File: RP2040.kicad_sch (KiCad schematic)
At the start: 19 parts, among them U1 RP2040, Y1 12MHz

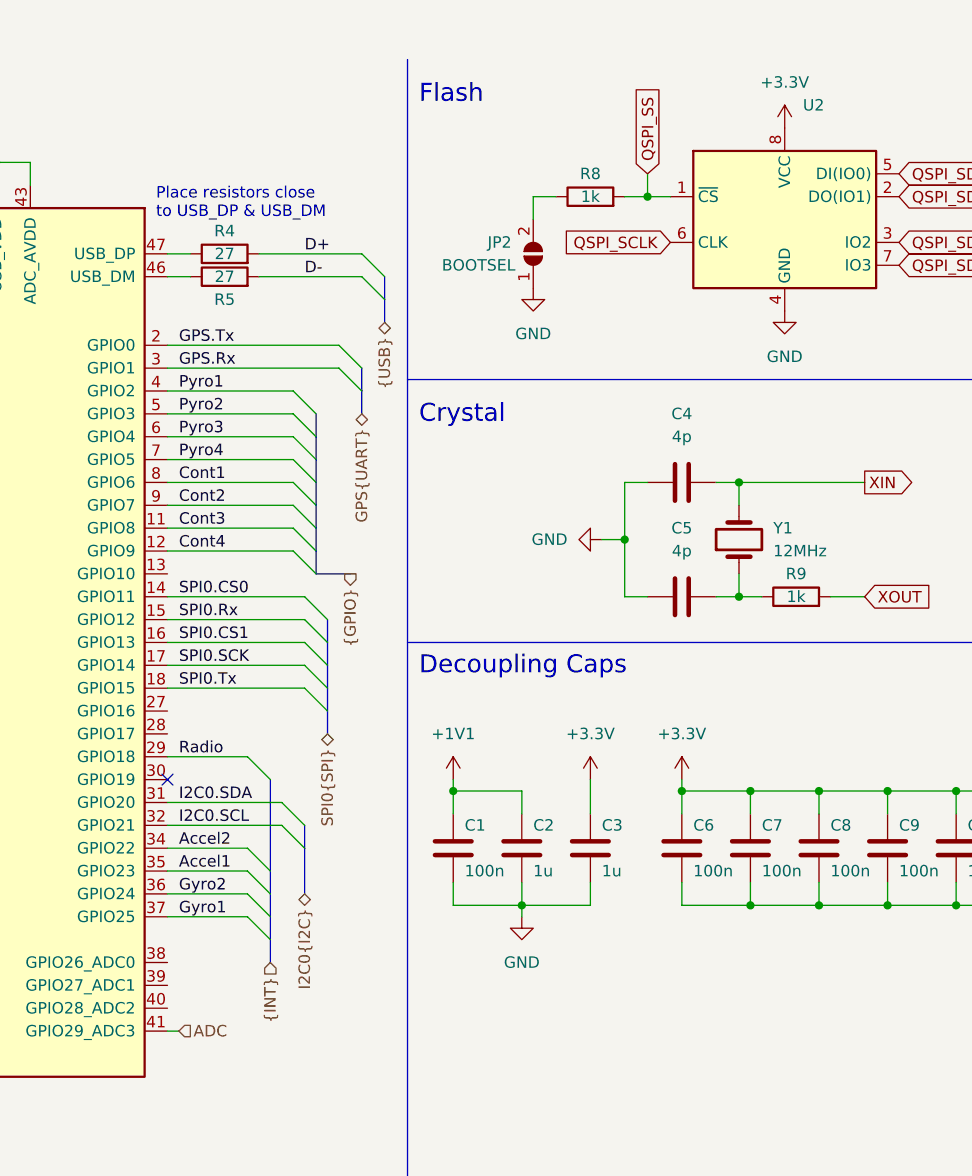
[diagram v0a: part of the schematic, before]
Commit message: Added polyfuse
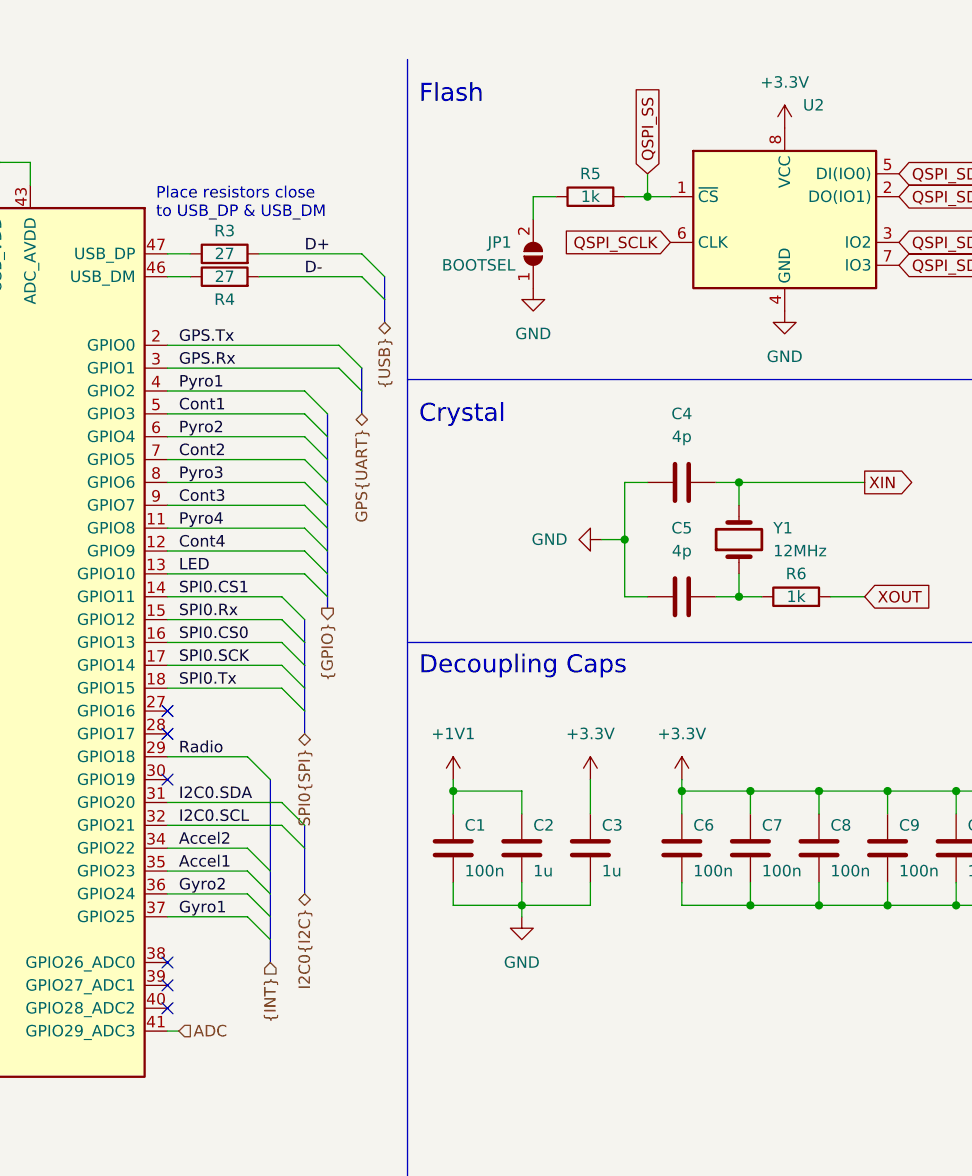
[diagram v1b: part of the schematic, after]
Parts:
- renumbered JP2 to JP1, R4 to R3, R5 to R4, R8 to R5, R9 to R6
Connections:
- net Cont1: now also U1.5 (GPIO3); no longer U1.8 (GPIO6)
- net Cont2: now also U1.7 (GPIO5); no longer U1.9 (GPIO7)
- net Cont3: now also U1.9 (GPIO7); no longer U1.11 (GPIO8)
- net Pyro2: now also U1.6 (GPIO4); no longer U1.5 (GPIO3)
- net Pyro3: now also U1.8 (GPIO6); no longer U1.6 (GPIO4)
- net Pyro4: now also U1.11 (GPIO8); no longer U1.7 (GPIO5)
- net SPI0.CS0: now also U1.16 (GPIO13); no longer U1.14 (GPIO11)
- net SPI0.CS1: now also U1.14 (GPIO11); no longer U1.16 (GPIO13)
- net LED: now reaches U1.13 (GPIO10)
- no-connect marks 5 -> 10

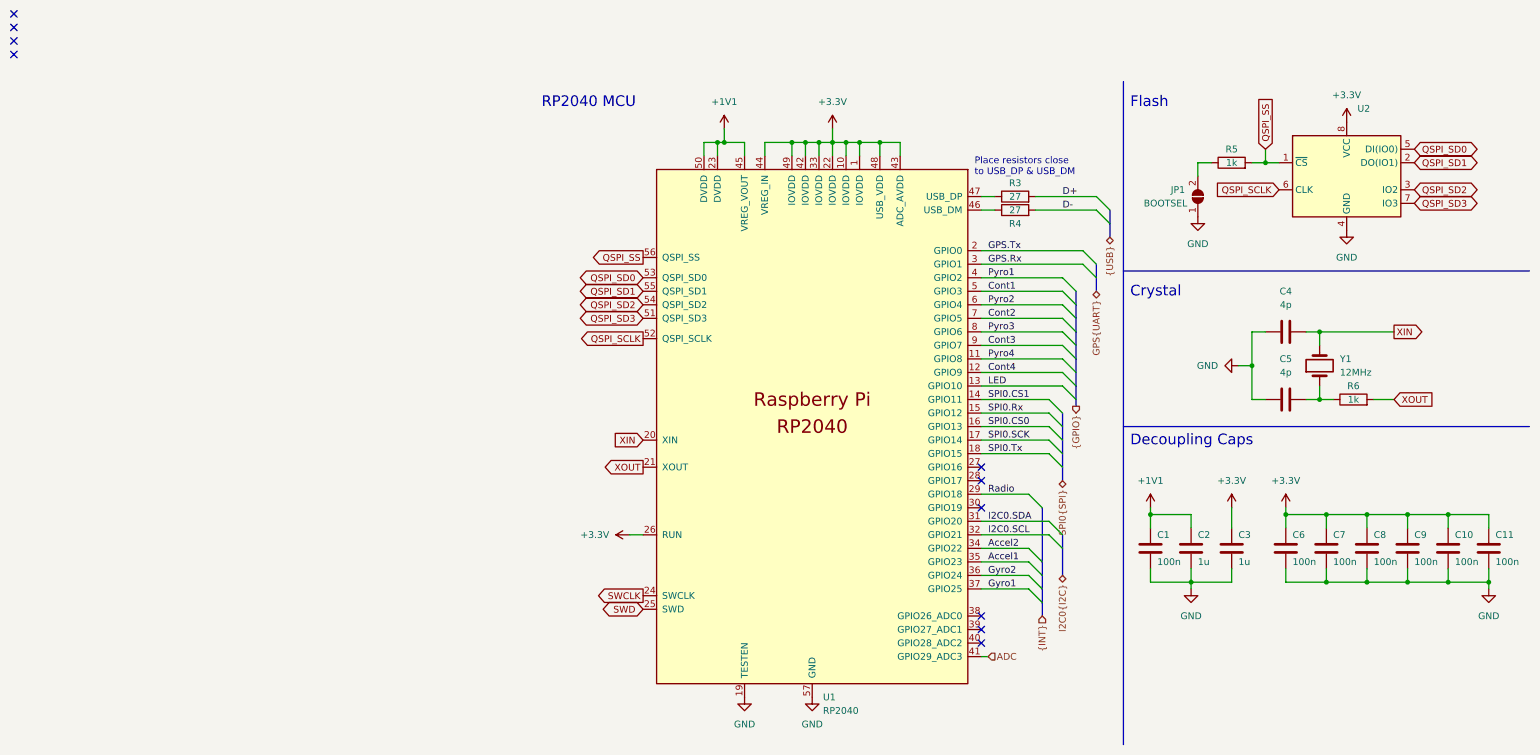
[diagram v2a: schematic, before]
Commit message: Centered RP2040, added mounting hardware, Rearranged radio
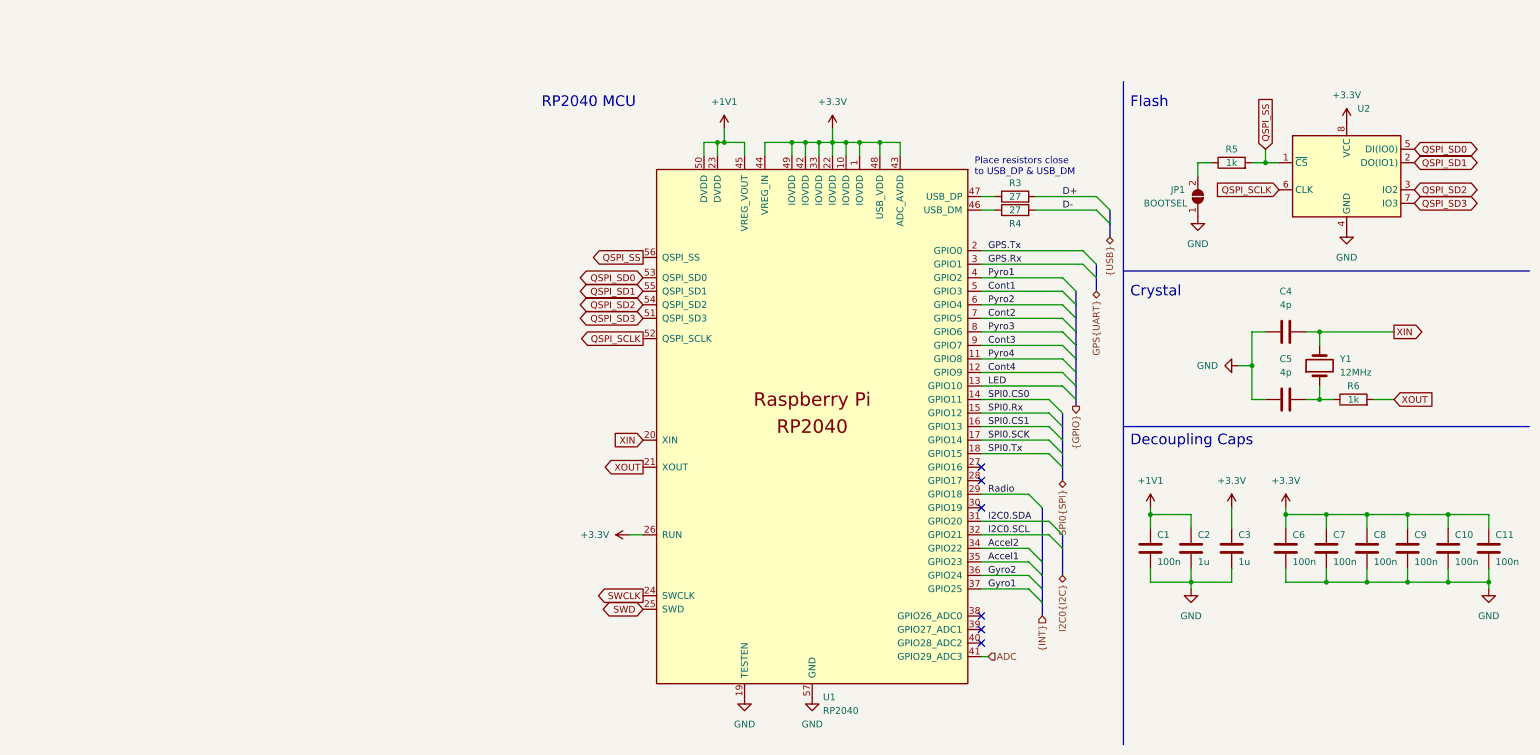
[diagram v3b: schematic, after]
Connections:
- net SPI0.CS0: now also U1.14 (GPIO11); no longer U1.16 (GPIO13)
- net SPI0.CS1: now also U1.16 (GPIO13); no longer U1.14 (GPIO11)
- no-connect marks 10 -> 6
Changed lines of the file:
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@@
   (junction (at 46.99 22.86) (diameter 0) (color 0 0 0 0)
   )
-  (no_connect (at -86.36 1.27))
   (no_connect (at 95.25 91.44))
-  (no_connect (at -86.36 -1.27))
-  (no_connect (at -86.36 3.81))
-  (no_connect (at -86.36 6.35))
   (no_connect (at 95.25 111.76))
   (no_connect (at 95.25 114.3))
@@
     (effects (font (size 1.27 1.27)) (justify left bottom))
   )
-  (label "SPI0.CS1" (at 96.52 71.12 0)
+  (label "SPI0.CS0" (at 96.52 71.12 0)
     (effects (font (size 1.27 1.27)) (justify left bottom))
   )
@@
     (effects (font (size 1.27 1.27)) (justify left bottom))
   )
-  (label "SPI0.CS0" (at 96.52 76.2 0)
+  (label "SPI0.CS1" (at 96.52 76.2 0)
     (effects (font (size 1.27 1.27)) (justify left bottom))
   )
@@
   (symbol (lib_id "power:GND") (at 190.5 106.68 0) (unit 1)
     (in_bom yes) (on_board yes) (fields_autoplaced)
-    (property "Reference" "#PWR015" (id 0) (at 190.5 113.03 0)
+    (property "Reference" "#PWR019" (id 0) (at 190.5 113.03 0)
       (effects (font (size 1.27 1.27)) hide)
     )
@@
   (symbol (lib_id "power:+3.3V") (at 152.4 91.44 0) (unit 1)
     (in_bom yes) (on_board yes) (fields_autoplaced)
-    (property "Reference" "#PWR012" (id 0) (at 152.4 95.25 0)
+    (property "Reference" "#PWR016" (id 0) (at 152.4 95.25 0)
       (effects (font (size 1.27 1.27)) hide)
     )
@@
   (symbol (lib_id "power:+1V1") (at 46.99 20.32 0) (unit 1)
     (in_bom yes) (on_board yes) (fields_autoplaced)
-    (property "Reference" "#PWR03" (id 0) (at 46.99 24.13 0)
+    (property "Reference" "#PWR07" (id 0) (at 46.99 24.13 0)
       (effects (font (size 1.27 1.27)) hide)
     )
@@
   (symbol (lib_id "power:+3.3V") (at 163.83 19.05 0) (unit 1)
     (in_bom yes) (on_board yes) (fields_autoplaced)
-    (property "Reference" "#PWR013" (id 0) (at 163.83 22.86 0)
+    (property "Reference" "#PWR017" (id 0) (at 163.83 22.86 0)
       (effects (font (size 1.27 1.27)) hide)
     )
@@
   (symbol (lib_id "power:+3.3V") (at 29.21 96.52 90) (unit 1)
     (in_bom yes) (on_board yes) (fields_autoplaced)
-    (property "Reference" "#PWR02" (id 0) (at 33.02 96.52 0)
+    (property "Reference" "#PWR06" (id 0) (at 33.02 96.52 0)
       (effects (font (size 1.27 1.27)) hide)
     )
@@
   (symbol (lib_id "power:GND") (at 135.89 36.83 0) (unit 1)
     (in_bom yes) (on_board yes) (fields_autoplaced)
-    (property "Reference" "#PWR09" (id 0) (at 135.89 43.18 0)
+    (property "Reference" "#PWR013" (id 0) (at 135.89 43.18 0)
       (effects (font (size 1.27 1.27)) hide)
     )
@@
   (symbol (lib_id "power:GND") (at 163.83 39.37 0) (unit 1)
     (in_bom yes) (on_board yes) (fields_autoplaced)
-    (property "Reference" "#PWR014" (id 0) (at 163.83 45.72 0)
+    (property "Reference" "#PWR018" (id 0) (at 163.83 45.72 0)
       (effects (font (size 1.27 1.27)) hide)
     )
@@
   (symbol (lib_id "power:+3.3V") (at 67.31 20.32 0) (unit 1)
     (in_bom yes) (on_board yes) (fields_autoplaced)
-    (property "Reference" "#PWR06" (id 0) (at 67.31 24.13 0)
+    (property "Reference" "#PWR010" (id 0) (at 67.31 24.13 0)
       (effects (font (size 1.27 1.27)) hide)
     )
@@
   (symbol (lib_id "power:GND") (at 63.5 127 0) (unit 1)
     (in_bom yes) (on_board yes) (fields_autoplaced)
-    (property "Reference" "#PWR05" (id 0) (at 63.5 133.35 0)
+    (property "Reference" "#PWR09" (id 0) (at 63.5 133.35 0)
       (effects (font (size 1.27 1.27)) hide)
     )
@@
   (symbol (lib_id "power:+1V1") (at 127 91.44 0) (unit 1)
     (in_bom yes) (on_board yes)
-    (property "Reference" "#PWR07" (id 0) (at 127 95.25 0)
+    (property "Reference" "#PWR011" (id 0) (at 127 95.25 0)
       (effects (font (size 1.27 1.27)) hide)
     )
@@
   (symbol (lib_id "power:GND") (at 50.8 127 0) (unit 1)
     (in_bom yes) (on_board yes) (fields_autoplaced)
-    (property "Reference" "#PWR04" (id 0) (at 50.8 133.35 0)
+    (property "Reference" "#PWR08" (id 0) (at 50.8 133.35 0)
       (effects (font (size 1.27 1.27)) hide)
     )
@@
   (symbol (lib_id "power:GND") (at 143.51 64.77 270) (unit 1)
     (in_bom yes) (on_board yes) (fields_autoplaced)
-    (property "Reference" "#PWR011" (id 0) (at 137.16 64.77 0)
+    (property "Reference" "#PWR015" (id 0) (at 137.16 64.77 0)
       (effects (font (size 1.27 1.27)) hide)
     )
@@
   (symbol (lib_id "power:GND") (at 134.62 106.68 0) (unit 1)
     (in_bom yes) (on_board yes) (fields_autoplaced)
-    (property "Reference" "#PWR08" (id 0) (at 134.62 113.03 0)
+    (property "Reference" "#PWR012" (id 0) (at 134.62 113.03 0)
       (effects (font (size 1.27 1.27)) hide)
     )
@@
   (symbol (lib_id "power:+3.3V") (at 142.24 91.44 0) (unit 1)
     (in_bom yes) (on_board yes) (fields_autoplaced)
-    (property "Reference" "#PWR010" (id 0) (at 142.24 95.25 0)
-      (effects (font (size 1.27 1.27)) hide)
-    )
+    (property "Reference" "#PWR014" (id 0) (at 142.24 95.25 0)
+      (effects (font (size 1.27 1.27)) hide)
+    )

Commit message: Geographical reannotated
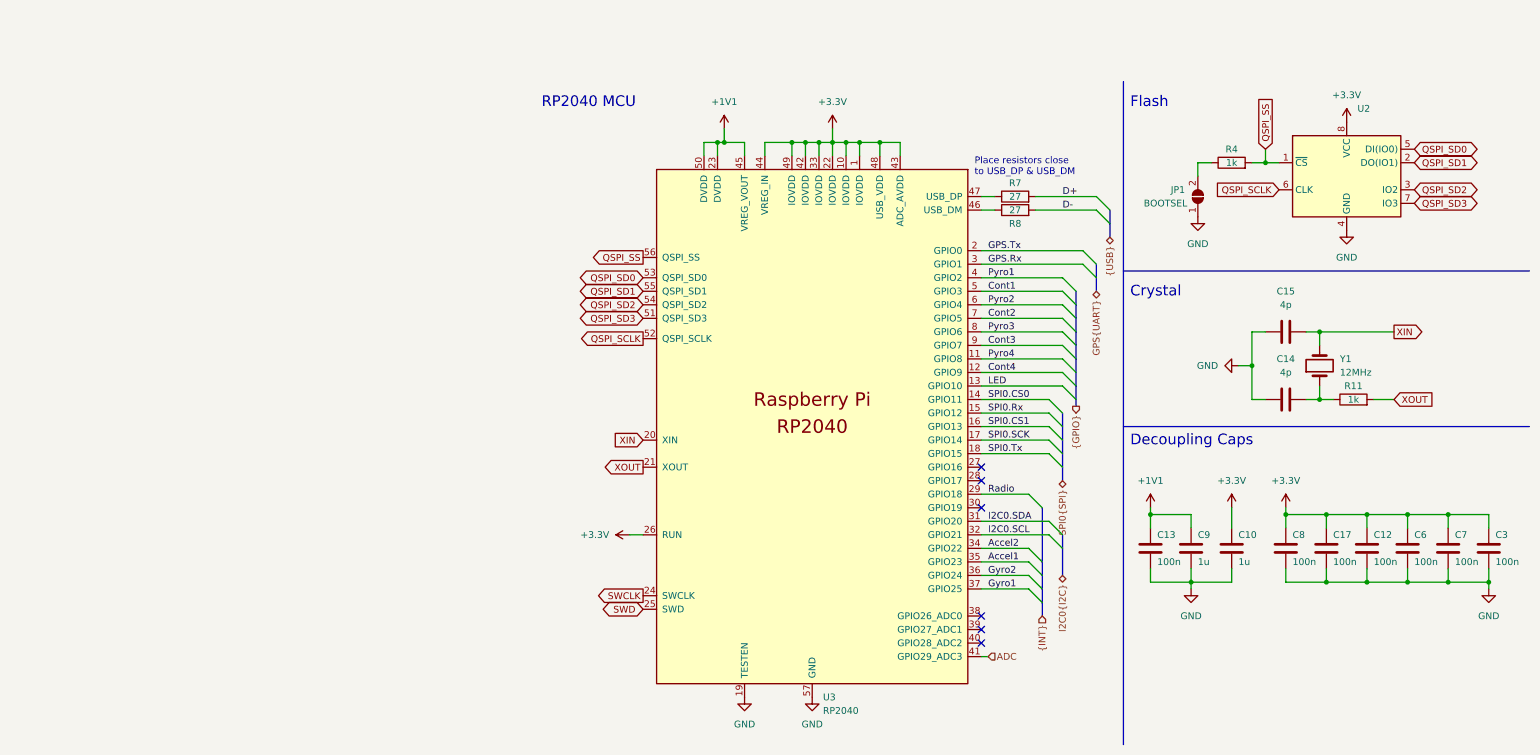
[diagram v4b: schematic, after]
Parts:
- renumbered C3 to C10, C8 to C12, C1 to C13, C5 to C14, C4 to C15, C7 to C17, C11 to C3, C9 to C6, C10 to C7, C6 to C8, C2 to C9, R6 to R11, R5 to R4, R3 to R7, R4 to R8, U1 to U3
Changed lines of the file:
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@@
   (symbol (lib_id "Device:C") (at 160.02 99.06 0) (unit 1)
     (in_bom yes) (on_board yes)
-    (property "Reference" "C7" (id 0) (at 161.29 96.52 0)
+    (property "Reference" "C17" (id 0) (at 161.29 96.52 0)
       (effects (font (size 1.27 1.27)) (justify left))
     )
@@
   (symbol (lib_id "Device:R") (at 165.1 71.12 90) (unit 1)
     (in_bom yes) (on_board yes)
-    (property "Reference" "R6" (id 0) (at 165.1 68.58 90))
+    (property "Reference" "R11" (id 0) (at 165.1 68.58 90))
     (property "Value" "1k" (id 1) (at 165.1 71.12 90))
     (property "Footprint" "Resistor_SMD:R_0603_1608Metric" (id 2) (at 165.1 72.898 90)
@@
   (symbol (lib_id "Device:C") (at 152.4 71.12 90) (unit 1)
     (in_bom yes) (on_board yes) (fields_autoplaced)
-    (property "Reference" "C5" (id 0) (at 152.4 63.5 90))
+    (property "Reference" "C14" (id 0) (at 152.4 63.5 90))
     (property "Value" "4p" (id 1) (at 152.4 66.04 90))
     (property "Footprint" "Capacitor_SMD:C_0603_1608Metric" (id 2) (at 156.21 70.1548 0)
@@
   (symbol (lib_id "Device:C") (at 142.24 99.06 0) (unit 1)
     (in_bom yes) (on_board yes)
-    (property "Reference" "C3" (id 0) (at 143.51 96.52 0)
+    (property "Reference" "C10" (id 0) (at 143.51 96.52 0)
       (effects (font (size 1.27 1.27)) (justify left))
     )
@@
   (symbol (lib_id "Device:C") (at 152.4 99.06 0) (unit 1)
     (in_bom yes) (on_board yes)
-    (property "Reference" "C6" (id 0) (at 153.67 96.52 0)
+    (property "Reference" "C8" (id 0) (at 153.67 96.52 0)
       (effects (font (size 1.27 1.27)) (justify left))
     )
@@
   (symbol (lib_id "Device:C") (at 182.88 99.06 0) (unit 1)
     (in_bom yes) (on_board yes)
-    (property "Reference" "C10" (id 0) (at 184.15 96.52 0)
+    (property "Reference" "C7" (id 0) (at 184.15 96.52 0)
       (effects (font (size 1.27 1.27)) (justify left))
     )
@@
   (symbol (lib_id "Device:R") (at 101.6 33.02 90) (unit 1)
     (in_bom yes) (on_board yes)
-    (property "Reference" "R3" (id 0) (at 101.6 30.48 90))
+    (property "Reference" "R7" (id 0) (at 101.6 30.48 90))
     (property "Value" "27" (id 1) (at 101.6 33.02 90))
     (property "Footprint" "Resistor_SMD:R_0603_1608Metric_Pad0.98x0.95mm_HandSolder" (id 2) (at 101.6 34.798 90)
@@
   (symbol (lib_id "Device:R") (at 101.6 35.56 90) (unit 1)
     (in_bom yes) (on_board yes)
-    (property "Reference" "R4" (id 0) (at 101.6 38.1 90))
+    (property "Reference" "R8" (id 0) (at 101.6 38.1 90))
     (property "Value" "27" (id 1) (at 101.6 35.56 90))
     (property "Footprint" "Resistor_SMD:R_0603_1608Metric_Pad0.98x0.95mm_HandSolder" (id 2) (at 101.6 37.338 90)
@@
   (symbol (lib_id "Device:R") (at 142.24 26.67 90) (unit 1)
     (in_bom yes) (on_board yes)
-    (property "Reference" "R5" (id 0) (at 142.24 24.13 90))
+    (property "Reference" "R4" (id 0) (at 142.24 24.13 90))
     (property "Value" "1k" (id 1) (at 142.24 26.67 90))
     (property "Footprint" "Resistor_SMD:R_0603_1608Metric" (id 2) (at 142.24 28.448 90)
@@
   (symbol (lib_id "Device:C") (at 167.64 99.06 0) (unit 1)
     (in_bom yes) (on_board yes)
-    (property "Reference" "C8" (id 0) (at 168.91 96.52 0)
+    (property "Reference" "C12" (id 0) (at 168.91 96.52 0)
       (effects (font (size 1.27 1.27)) (justify left))
     )
@@
   (symbol (lib_id "Device:C") (at 134.62 99.06 0) (unit 1)
     (in_bom yes) (on_board yes)
-    (property "Reference" "C2" (id 0) (at 135.89 96.52 0)
+    (property "Reference" "C9" (id 0) (at 135.89 96.52 0)
       (effects (font (size 1.27 1.27)) (justify left))
     )
@@
   (symbol (lib_id "Device:C") (at 127 99.06 0) (unit 1)
     (in_bom yes) (on_board yes)
-    (property "Reference" "C1" (id 0) (at 128.27 96.52 0)
+    (property "Reference" "C13" (id 0) (at 128.27 96.52 0)
       (effects (font (size 1.27 1.27)) (justify left))
     )
@@
   (symbol (lib_id "Device:C") (at 190.5 99.06 0) (unit 1)
     (in_bom yes) (on_board yes)
-    (property "Reference" "C11" (id 0) (at 191.77 96.52 0)
+    (property "Reference" "C3" (id 0) (at 191.77 96.52 0)
       (effects (font (size 1.27 1.27)) (justify left))
     )
@@
   (symbol (lib_id "Device:C") (at 175.26 99.06 0) (unit 1)
     (in_bom yes) (on_board yes)
-    (property "Reference" "C9" (id 0) (at 176.53 96.52 0)
+    (property "Reference" "C6" (id 0) (at 176.53 96.52 0)
       (effects (font (size 1.27 1.27)) (justify left))
     )
@@
   (symbol (lib_id "Device:C") (at 152.4 58.42 90) (unit 1)
     (in_bom yes) (on_board yes) (fields_autoplaced)
-    (property "Reference" "C4" (id 0) (at 152.4 50.8 90))
+    (property "Reference" "C15" (id 0) (at 152.4 50.8 90))
     (property "Value" "4p" (id 1) (at 152.4 53.34 90))
     (property "Footprint" "Capacitor_SMD:C_0603_1608Metric" (id 2) (at 156.21 57.4548 0)
@@
   (symbol (lib_id "YAR_MCU:RP2040") (at 63.5 76.2 0) (unit 1)
     (in_bom yes) (on_board yes) (fields_autoplaced)
-    (property "Reference" "U1" (id 0) (at 65.5194 127 0)
-      (effects (font (size 1.27 1.27)) (justify left))
-    )
+    (property "Reference" "U3" (id 0) (at 65.5194 127 0)
+      (effects (font (size 1.27 1.27)) (justify left))
+    )
